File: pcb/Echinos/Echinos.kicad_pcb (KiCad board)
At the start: 2 copper layers, 167.4 x 137.9 mm, 131 parts, among them J1 Conn_01x06_Socket, J2 Conn_01x06_Socket, J3 Conn_01x06_Socket, J6 USB_B_Micro, J7 Conn_01x04_Socket, J8 USB_C_Receptacle_USB2.0, SW1 Reset, SW111 SW_Push, SW112 SW_Push, SW113 SW_Push, SW114 SW_Push, SW115 SW_Push, SW122 SW_Push, SW123 SW_Push, SW124 SW_Push, SW125 SW_Push, SW131 SW_Push, SW132 SW_Push, SW133 SW_Push, SW134 SW_Push, SW135 SW_Push, SW141 SW_Push, SW142 SW_Push, SW143 SW_Push, SW144 SW_Push, SW145 SW_Push, SW151 SW_Push, SW152 SW_Push, SW153 SW_Push, SW154 SW_Push, SW155 SW_Push, SW2 SW_Push, SW3 SW_Push, U1 Helios, U2 USBLC6-2P6, U3 XC6210B332MR-G, U4 W25Q128JVS, U5 RP2040, U7 USBLC6-2P6, X1 CMOS -12MHz

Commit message: [PCB] - Save last state with on board RP2040.
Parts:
- removed D2: 1N4148, Diode_SMD:D_SOD-323_HandSoldering
- removed SW1: Reset, Button_Switch_SMD:SW_SPST_TL3342
- removed U1: Helios, Echinos:Helios_AH_USBup
- added J5: Conn_01x05_Socket, Connector_PinHeader_2.00mm:PinHeader_1x05_P2.00mm_Vertical, F.Cu at (109.3, 143.7)
- added SW4: Reset, Button_Switch_SMD:SW_SPST_TS-1088-xR020, B.Cu at (103.1, 153.9)
- added SW5: SW_Push, Button_Switch_SMD:SW_SPST_TS-1088-xR020, B.Cu at (95.9, 153.9)
- added U8: 74LVC1T45, Package_TO_SOT_SMD:SOT-563, B.Cu at (68.0, 150.2)
- JP0, JP11: footprint Jumper:SolderJumper-2_P1.3mm_Bridged_Pad1.0x1.5mm -> Jumper:SolderJumper-2_P1.3mm_Bridged_RoundedPad1.0x1.5mm
- JP12: footprint Jumper:SolderJumper-3_P1.3mm_Bridged12_Pad1.0x1.5mm_NumberLabels -> Jumper:SolderJumper-3_P1.3mm_Bridged12_RoundedPad1.0x1.5mm_NumberLabels
- JP13, JP14, JP15, JP16: footprint Jumper:SolderJumper-2_P1.3mm_Open_Pad1.0x1.5mm -> Jumper:SolderJumper-2_P1.3mm_Open_RoundedPad1.0x1.5mm
- JP205: footprint Echinos:SolderJumper_Open_0.8x1.2mm -> Jumper:SolderJumper-2_P1.3mm_Bridged_RoundedPad1.0x1.5mm; moved to F.Cu
- SW2: footprint Button_Switch_SMD:SW_SPST_CK_KXT3 -> Button_Switch_SMD:SW_SPST_TS-1088-xR020; moved to F.Cu
- SW3: value SW_Push -> Reset; footprint Button_Switch_SMD:SW_SPST_CK_KXT3 -> Button_Switch_SMD:SW_SPST_TS-1088-xR020; moved to F.Cu
- moved C6 171.6 mm to (108.4, 153.9)
- moved SW3 170.3 mm to (103.1, 153.9)
- moved R5 169.0 mm to (105.7, 150.0)
- moved JP14 123.7 mm to (98.1, 148.5), turned to 180 degrees
- moved JP13 123.0 mm to (98.1, 145.2), turned to 180 degrees
- moved R14 116.0 mm to (94.2, 148.2), turned to 0 degrees
- moved R13 115.4 mm to (94.2, 145.5), turned to 0 degrees
- moved R9 115.0 mm to (68.6, 89.7), turned to -90 degrees
- moved JP205 112.5 mm to (65.0, 95.5), turned to 90 degrees
- moved D1 109.9 mm to (63.5, 81.3)
- moved JP12 106.2 mm to (74.8, 149.7), turned to -90 degrees
- moved R16 99.7 mm to (65.4, 147.6), turned to -90 degrees
- moved JP11 98.6 mm to (71.7, 149.7), turned to 0 degrees
- moved JP16 96.2 mm to (65.0, 151.2), turned to 90 degrees
- moved R15 95.6 mm to (61.6, 147.6), turned to -90 degrees
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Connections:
- C6 pad 1: /RP2040/~{RST} -> reset
- J1 pad 1: row6 -> col5
- J1 pad 2: col1 -> col4
- J1 pad 3: col2 -> col3
- J1 pad 4: col3 -> col2
- J1 pad 5: col4 -> col1
- J1 pad 6: col5 -> row6
- J2 pad 6: col2 -> col6
- JP11 pad 1: rgb -> rgb_5V
- R10 pad 1: /USB_D+ -> /USB+
- R11 pad 1: /USB_D- -> /USB-
- R5 pad 2: /RP2040/~{RST} -> reset
- SW3 pad 1: /RP2040/~{RST} -> reset
- U5 pad 12: row1 -> col1
- U5 pad 13: ps2_reset -> row1
- U5 pad 14: row7 -> row2
- U5 pad 15: col1 -> /RP2040/GPIO12
- U5 pad 16: sda1 -> row6
- U5 pad 17: scl1 -> sda1
- U5 pad 18: row6 -> scl1
- U5 pad 24: /RP2040/SWCLK -> swclk
- U5 pad 25: /RP2040/SWDIO -> swdio
- U5 pad 26: /RP2040/~{RST} -> reset
- U5 pad 27: row2 -> col6
- U5 pad 28: /RP2040/GPIO17 -> row7
- U5 pad 36: /RP2040/GPIO24 -> rgb
- U5 pad 37: rgb -> ps2_reset
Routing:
- net +3.3V: track 89.9 -> 203.4 mm, vias 3 -> 17
- net /RP2040/QSPI_SS: track 0.00 -> 59.3 mm, vias 0 -> 4
- net row7: track 62.9 -> 7.66 mm, vias 2 -> 0
- net RX: track 2.94 -> 52.4 mm
- net VBUS: track 26.5 -> 74.1 mm, vias 1 -> 2
- net TX: track 4.20 -> 51.3 mm
- net /Backlight/backlight_in: track 14.3 -> 60.9 mm
- net reset: track 10.5 -> 57.1 mm, vias 0 -> 2
- net swdio: track 0.00 -> 44.8 mm
- net swclk: track 0.00 -> 44.1 mm
- net +5V: track 469.9 -> 508.5 mm, vias 8 -> 12
- net scl1: track 11.0 -> 49.4 mm, vias 0 -> 3
- net sda1: track 11.9 -> 48.8 mm, vias 0 -> 3
- net GND: track 50.9 -> 82.6 mm, vias 52 -> 257
- net row6: track 30.0 -> 60.5 mm, vias 1 -> 2
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- added copper zone on B.Cu, net +3.3V
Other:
- outline, holes or cut-outs redrawn

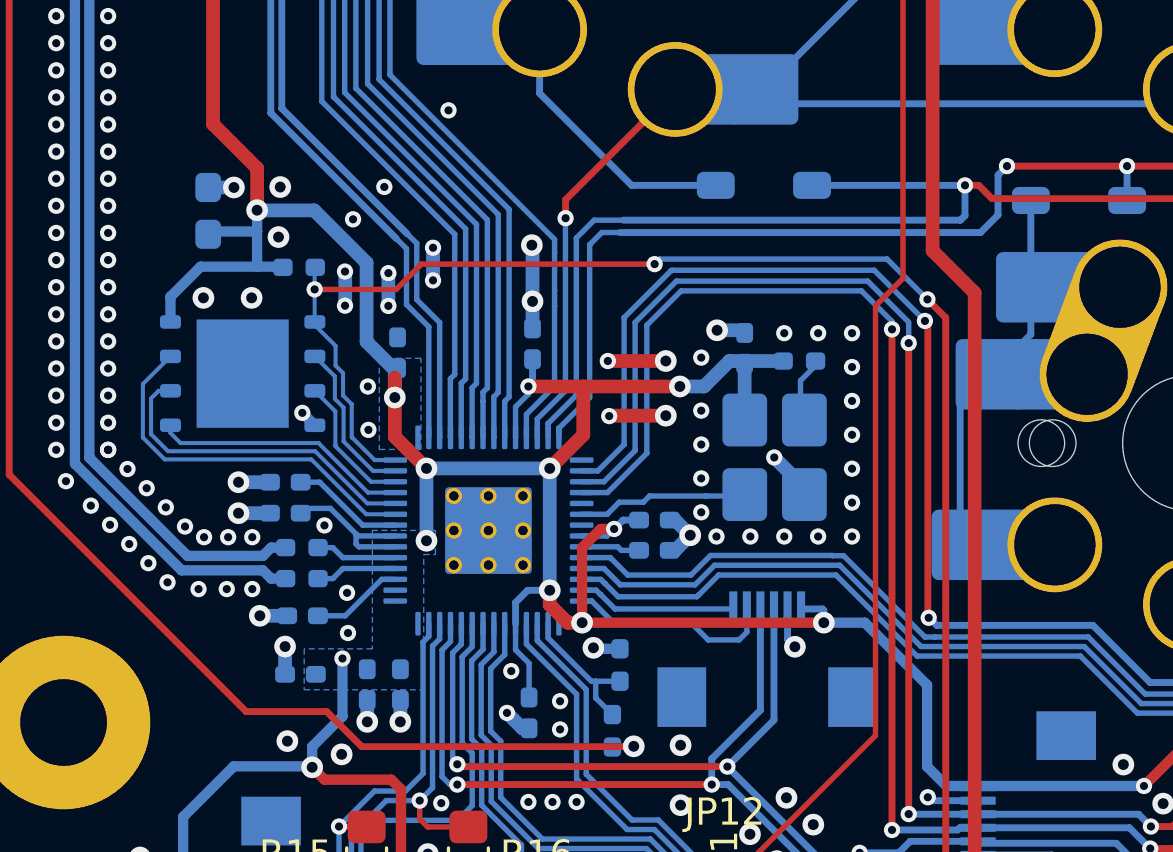
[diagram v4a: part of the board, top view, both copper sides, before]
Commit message: [PCB] - Save last state with on board RP2040.   - Route crystal and 1V1
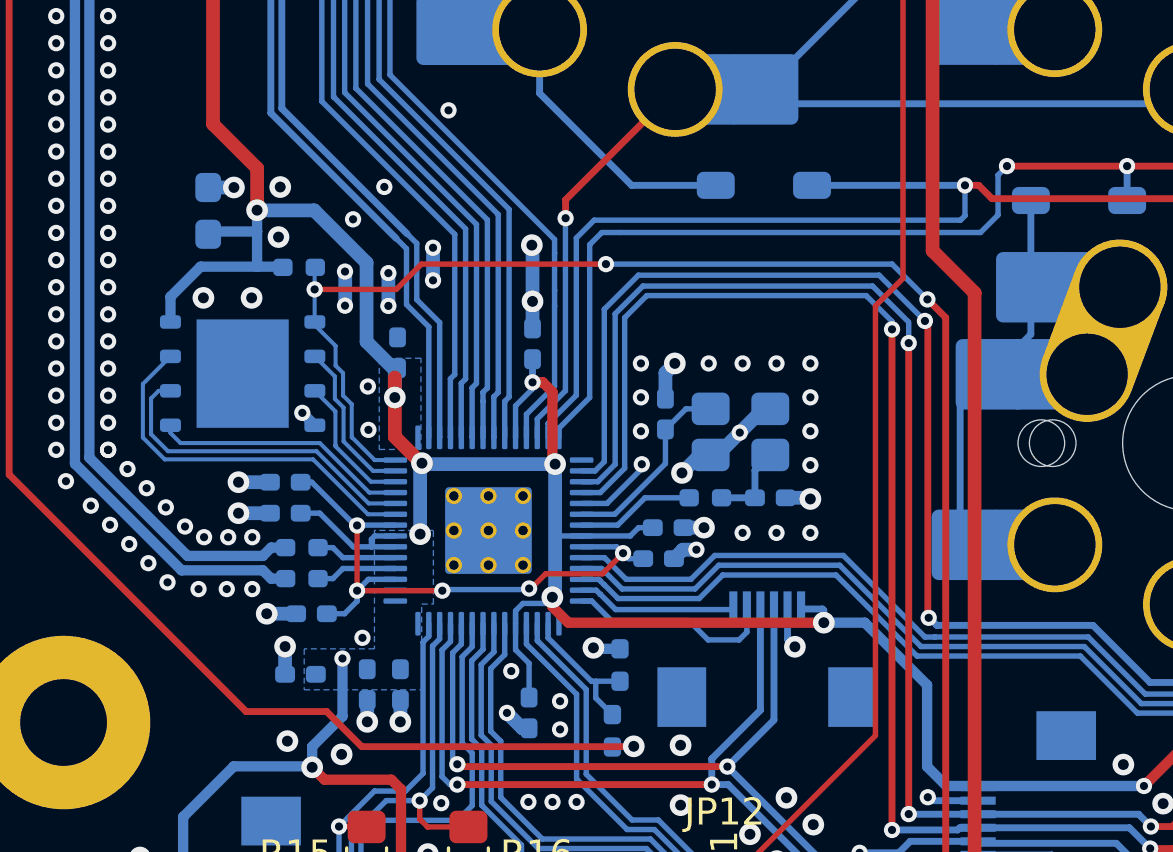
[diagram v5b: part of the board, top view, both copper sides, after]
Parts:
- removed X1: CMOS -12MHz, Oscillator:Oscillator_SMD_Abracon_ASE-4Pin_3.2x2.5mm_HandSoldering
- added C25: 15pF, Capacitor_SMD:C_0402_1005Metric_Pad0.74x0.62mm_HandSolder, B.Cu at (76.5, 134.4)
- added Y2: Crystal_GND24, Crystal:Crystal_SMD_Abracon_ABM8G-4Pin_3.2x2.5mm, B.Cu at (75.4, 132.0)
- C5: value 0.1µF -> 15pF
- R6: value 10k -> 1k
- moved R6 6.12 mm to (74.1, 134.4), turned to 0 degrees
- moved C5 3.80 mm to (72.6, 131.3), turned to -90 degrees
- moved C19 0.58 mm to (72.7, 135.5)
- moved C7 0.34 mm to (72.4, 136.7)
- moved C9 0.34 mm to (59.6, 138.7)
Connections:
- C5 pad 1: +3.3V -> GND
- C5 pad 2: GND -> Net-(U5-XIN)
- R6 pad 1: Net-(X1-EN) -> Net-(U5-XOUT)
- R6 pad 2: +3.3V -> Net-(C25-Pad2)
- U5 pad 21: unconnected-(U5-XOUT-Pad21) -> Net-(U5-XOUT)
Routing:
- net +3.3V: track 203.4 -> 188.0 mm, vias 17 -> 14
- net +1V1: track 9.72 -> 22.8 mm, vias 0 -> 5
- net Net-(U5-XOUT): track 0.00 -> 4.38 mm
- net Net-(C25-Pad2): track 0.00 -> 3.05 mm
- net Net-(X1-EN): track 2.68 -> 0.00 mm
- net GND: track 82.6 -> 84.9 mm, vias 257 -> 250
- net Net-(U5-XIN): track 6.31 -> 7.11 mm
